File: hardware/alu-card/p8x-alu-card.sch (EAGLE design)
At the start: 32 parts, among them J1 DIN41612-96M, U1 A REG, U10 ALU HI, U11 CLA, U12 SH1 LO, U13 SH1 HI, U14 SH2 LO, U15 SH2 HI, U16 ALU OUT, U17 FLAGS, U18 Z DET, U19 74HCT08, U2 A OUT, U20 DOE DEC, U21 DLD DEC, U22 FLAG MUX, U23 FLAG OUT, U24 74HCT32, U25 74HCT00, U3 B REG, U4 B OUT, U5 T REG, U6 T OUT, U7 T2 REG, U8 T2 OUT, U9 ALU LO

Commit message: hw(rev B): ALU conventional-carry inverter; scope flag-reg redesign
Phase 2, step 4 (partial). The C flag is now conventional active-high:
the raw 74181 Cn+4 (active-low) is inverted by a spare U25 NAND gate
before the flag mux, matching the rev-B emulator/microcode.

The rest of the ALU rev-B work (LDZN independent Z/N latching, SETC/CLRC
forcing C, and the carry-coupled shifter) is one interlocking flag-
register redesign — it needs splitting C onto its own flip-flop and
source/clock muxes, ~6 chips that can only be pin-validated here, not
DRC'd. Scoped in detail in BACKLOG rather than bolted on unverified.
Functional behaviour is already proven in the emulator.

Co-Authored-By: Claude Opus 4.8 <noreply@anthropic.com>
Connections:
- new net CFLGI: U22.A1, U25.2Y
- net CFLG: now also U25.2A, U25.2B; no longer U22.A1
- net GND: no longer U25.2A, U25.2B
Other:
- note added: "P8X ALU CARD REV B-partial (carry conventional; flag-reg redesign pending - BACKLOG)"
- note removed: "P8X ALU CARD REV A (V FLAG UNIMPLEMENTED - SEE BACKLOG)"
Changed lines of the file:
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@@
 <part name="LED5" library="p8x" deviceset="LED" device="" value="LDF-YEL"/>
 </parts><sheets><sheet><plain>
-<text x="0" y="40" size="3.81" layer="97">P8X ALU CARD REV A (V FLAG UNIMPLEMENTED - SEE BACKLOG)</text>
+<text x="0" y="40" size="3.81" layer="97">P8X ALU CARD REV B-partial (carry conventional; flag-reg redesign pending - BACKLOG)</text>
 </plain><instances>
 <instance part="J1" gate="G$1" x="0" y="38.1"/>
@@
 <wire x1="259.38" y1="-251.46" x2="264.46" y2="-251.46" width="0.1524" layer="91"/>
 <label x="264.46" y="-250.95" size="1.778" layer="95"/></segment>
+<segment><pinref part="U25" gate="G$1" pin="2A"/>
+<wire x1="122.22" y1="-805.18" x2="117.14" y2="-805.18" width="0.1524" layer="91"/>
+<label x="117.14" y="-804.67" size="1.778" layer="95"/></segment>
+<segment><pinref part="U25" gate="G$1" pin="2B"/>
+<wire x1="122.22" y1="-807.72" x2="117.14" y2="-807.72" width="0.1524" layer="91"/>
+<label x="117.14" y="-807.21" size="1.778" layer="95"/></segment>
+</net>
+<net name="CFLGI" class="0">
+<segment><pinref part="U25" gate="G$1" pin="2Y"/>
+<wire x1="157.78" y1="-802.64" x2="162.86" y2="-802.64" width="0.1524" layer="91"/>
+<label x="162.86" y="-802.13" size="1.778" layer="95"/></segment>
 <segment><pinref part="U22" gate="G$1" pin="A1"/>
 <wire x1="223.82" y1="-662.94" x2="218.74" y2="-662.94" width="0.1524" layer="91"/>
@@
 <wire x1="427.02" y1="-678.18" x2="421.94" y2="-678.18" width="0.1524" layer="91"/>
 <label x="421.94" y="-677.67" size="1.778" layer="95"/></segment>
-<segment><pinref part="U25" gate="G$1" pin="2A"/>
-<wire x1="122.22" y1="-805.18" x2="117.14" y2="-805.18" width="0.1524" layer="91"/>
-<label x="117.14" y="-804.67" size="1.778" layer="95"/></segment>
-<segment><pinref part="U25" gate="G$1" pin="2B"/>
-<wire x1="122.22" y1="-807.72" x2="117.14" y2="-807.72" width="0.1524" layer="91"/>
-<label x="117.14" y="-807.21" size="1.778" layer="95"/></segment>
 <segment><pinref part="U25" gate="G$1" pin="4A"/>
 <wire x1="122.22" y1="-815.34" x2="117.14" y2="-815.34" width="0.1524" layer="91"/>

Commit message: hw(rev B): ALU flag-register redesign — completes Phase 2
Splits the flag register so the rev-B controls work in hardware:
- C flag on its own 7474 (U26), clocked CLK&LDF; SETC/CLRC drive its
  async preset/clear (via U25 NAND inverters + U31 AND with -RES).
- C source mux (U28/U29 74157): shifted-out bit (F7 if SH0, F0 if SH1)
  when shifting, else the inverted Cn+4 (conventional carry).
- shifter shift-in mux (U30 74157): current C when SHCIN else CIN.
- Z/N/V kept in U17 (74175), clocked CLK&(LDF|LDZN); on LDZN their source
  mux U22 selects a 74260 bus zero-detect (U27) and D7 instead of the ALU
  result, so loads set Z/N without disturbing C/V. The unused flag-restore
  (DLD=5) mux was repurposed for this.
ALU card retitled REV B; LDZN/SHCIN/SETC/CLRC added to its bus set.
Validates clean (pin/pad); behaviour proven in the emulator. BACKLOG
marks Phase 2 done; full Eagle DRC stays on VERIFY.

Co-Authored-By: Claude Opus 4.8 <noreply@anthropic.com>
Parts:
- added U26: C FLAG FF, p8x:7474
- added U27: BUS Z-DET, p8x:74260
- added U28: SHIFT-OUT MUX, p8x:74157
- added U29: C-SRC MUX, p8x:74157
- added U30: SHIN MUX, p8x:74157
- added U31: 74HCT08 CLK/FORCE, p8x:GATES14
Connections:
- net FM0 renamed ZSRC
- net FM1 renamed NSRC
- removed net -FREST: U21.Y5, U25.1A, U25.1B
- removed net CLKF: U17.CLK, U19.2Y
- removed net FEN: U19.2B, U24.1Y
- removed net FM2: U17.D3, U22.Y3
- removed net FM3: U17.D4, U22.Y4
- removed net FRESP: U22.S, U24.1B, U25.1Y
- new net -CCLR: U26.!1CLR, U31.3Y
- new net -CLRCb: U25.4Y, U31.3B
- new net -SETCb: U25.1Y, U26.!1PRE
- new net CLKFC: U26.1CLK, U31.1Y
- new net CLKFZN: U17.CLK, U31.2Y
- new net CLRC: J1.B27, U25.4A, U25.4B
- new net FENZN: U24.1Y, U31.2A
- new net LDZN: J1.C28, U22.S, U24.1B
- new net NC: U26.1D, U29.Y1
- new net SETC: J1.C30, U25.1A, U25.1B
- new net SHANY: U24.2Y, U29.S
- new net SHCIN: J1.C29, U30.S
- new net SHIN: U12.B1, U15.B4, U30.Y1
- new net SHOUT: U28.Y1, U29.B1
- new net ZBH: U19.2B, U27.Y2
- new net ZBL: U19.2A, U27.Y1
- new net ZBUS: U19.2Y, U22.B1
- net -RES: now also U31.3A
- net CFLGI: now also U29.A1; no longer U22.A1
- net CIN: now also U30.A1; no longer U12.B1, U15.B4
- net CLK: now also U31.1A, U31.2B; no longer U19.2A
- net D0: now also U27.A1; no longer U22.B1
- net D1: now also U27.B1; no longer U22.B2
- net D2: now also U27.C1; no longer U22.B3
- net D3: now also U27.D1; no longer U22.B4
- net D4: now also U27.E1
- net D5: now also U27.A2
- net D6: now also U27.B2
- net D7: now also U22.B2, U27.C2
- net F0: now also U28.A1
- net F7: now also U28.B1
- net FQC: now also U26.1Q, U30.B1; no longer U17.Q1
- net FQN: now also U17.Q2; no longer U17.Q3
- net FQV: now also U17.Q3; no longer U17.Q4
- net FQZ: now also U17.Q1; no longer U17.Q2
- net GND: now also U17.D3, U26.2CLK, U26.2D, U27.D2, U27.E2, U28.!G, U29.!G, U30.!G, U31.4A, U31.4B; no longer U22.A4, U24.2A, U24.2B, U25.4A, U25.4B
- net LDF: now also U31.1B
- net R7: now also U22.A2; no longer U22.A3
- net SH0: now also U24.2A, U28.S
- net SH1: now also U24.2B
- net VCC: now also U26.!2CLR, U26.!2PRE
- net ZFLG: now also U22.A1; no longer U22.A2
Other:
- note added: "P8X ALU CARD REV B (conventional carry, LDZN, SETC/CLRC, carry-coupled shifter)"
- note removed: "P8X ALU CARD REV B-partial (carry conventional; flag-reg redesign pending - BACKLOG)"
- moved on the sheet: LED3, LED4, LED5, R4, R5, RP1

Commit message: hw: per-IC 100nF decoupling caps on every card
card standards sec.5 requires a decoupling cap per IC; only the backplane had
them. gen_eagle's card() now generates one 100nF cap (CDn, C_DISC footprint)
per IC on the five plug-in cards, placed next to its IC and wired VCC<->GND;
the memory card's separate build does the same for U1-U9.

Caps added: control 18, regbank 44, alu 31, io 15, cf 8, memory 9. All 7
boards regenerate with 0 validation errors; card schematic PDFs refreshed.
Placement is approximate (caps sit just below each IC) pending Fusion routing.

Clears a pre-fab blocker from the backlog.

Co-Authored-By: Claude Opus 4.8 <noreply@anthropic.com>
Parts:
- added CD1, CD10, CD11, CD12, CD13, CD14, CD15, CD16, CD17, CD18, CD19, CD2, CD20, CD21, CD22, CD23, CD24, CD25, CD26, CD27, CD28, CD29, CD3, CD30, CD31, CD4, CD5, CD6, CD7, CD8, CD9: 100N, p8x:CAP
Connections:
- net GND: now also CD1.2, CD10.2, CD11.2, CD12.2, CD13.2, CD14.2, CD15.2, CD16.2, CD17.2, CD18.2, CD19.2, CD2.2, CD20.2, CD21.2, CD22.2, CD23.2, CD24.2, CD25.2, CD26.2, CD27.2, CD28.2, CD29.2, CD3.2, CD30.2, CD31.2, CD4.2, CD5.2, CD6.2, CD7.2, CD8.2, CD9.2
- net VCC: now also CD1.1, CD10.1, CD11.1, CD12.1, CD13.1, CD14.1, CD15.1, CD16.1, CD17.1, CD18.1, CD19.1, CD2.1, CD20.1, CD21.1, CD22.1, CD23.1, CD24.1, CD25.1, CD26.1, CD27.1, CD28.1, CD29.1, CD3.1, CD30.1, CD31.1, CD4.1, CD5.1, CD6.1, CD7.1, CD8.1, CD9.1

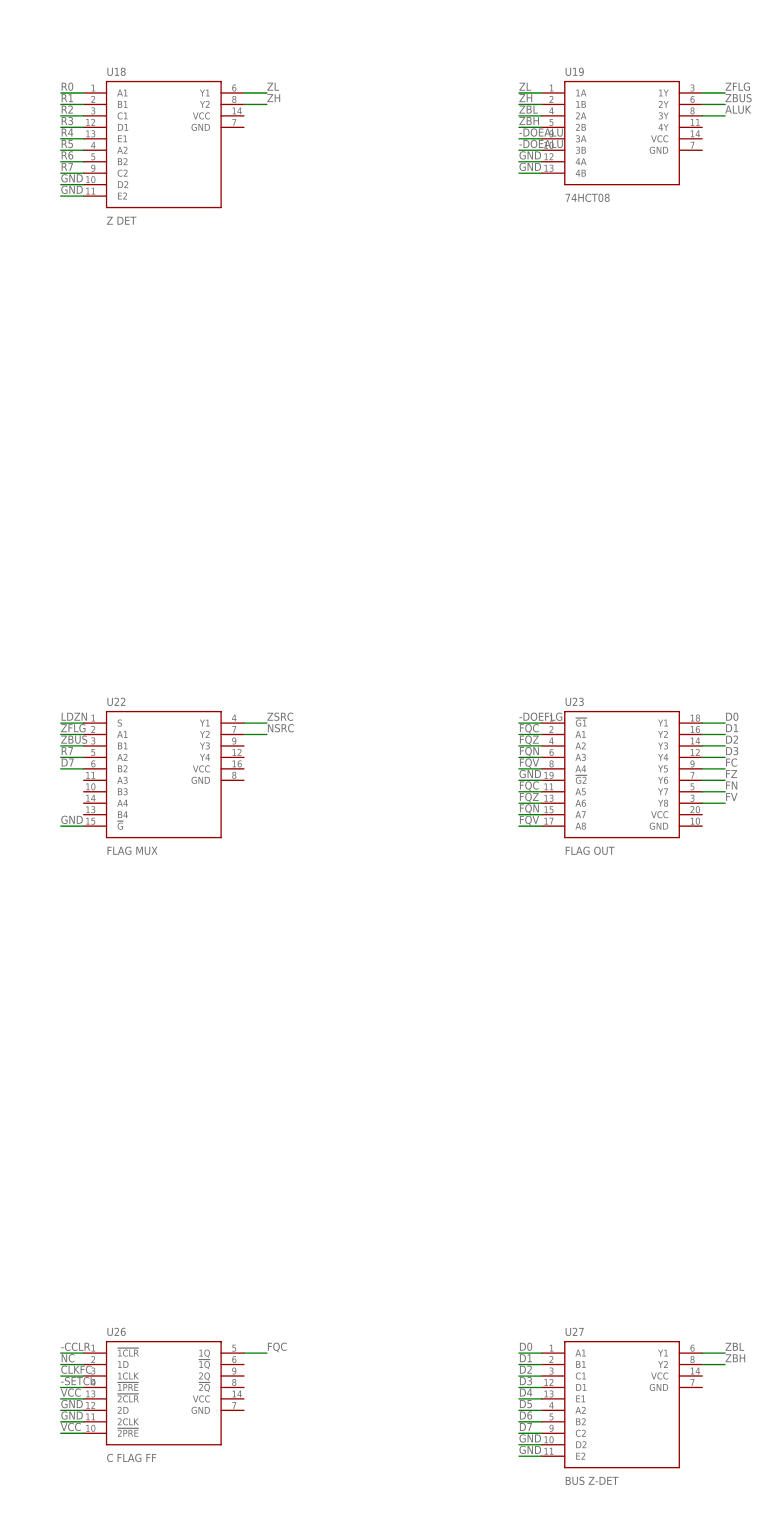
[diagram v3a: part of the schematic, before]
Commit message: hw: fix 74260 pinout (ALU zero-detect); datasheet pinout audit
Audited all ~25 device pin maps in gen_eagle's library against standard
datasheet pinouts. Found one real error: 74260 (dual 5-input NOR, used as the
ALU bus zero-detect U27) had a scrambled pin map — gate-1 C1 on pin 3 (should
be 11) and the Y1/Y2 outputs swapped (6<->8). Corrected to the datasheet
(1=1A 2=1B 3=2A 4=2B 5=2C 6=2Y 7=GND 8=1Y 9=2D 10=2E 11=1C 12=1D 13=1E 14=VCC);
netlist uses logical pin names so it's unchanged, and the zero-detect now wires
to the right pins. All other devices matched. Boards + PDFs regenerated, 0
validation errors.

Left a VERIFY note to confirm against physical datasheets before fab.

Co-Authored-By: Claude Opus 4.8 <noreply@anthropic.com>
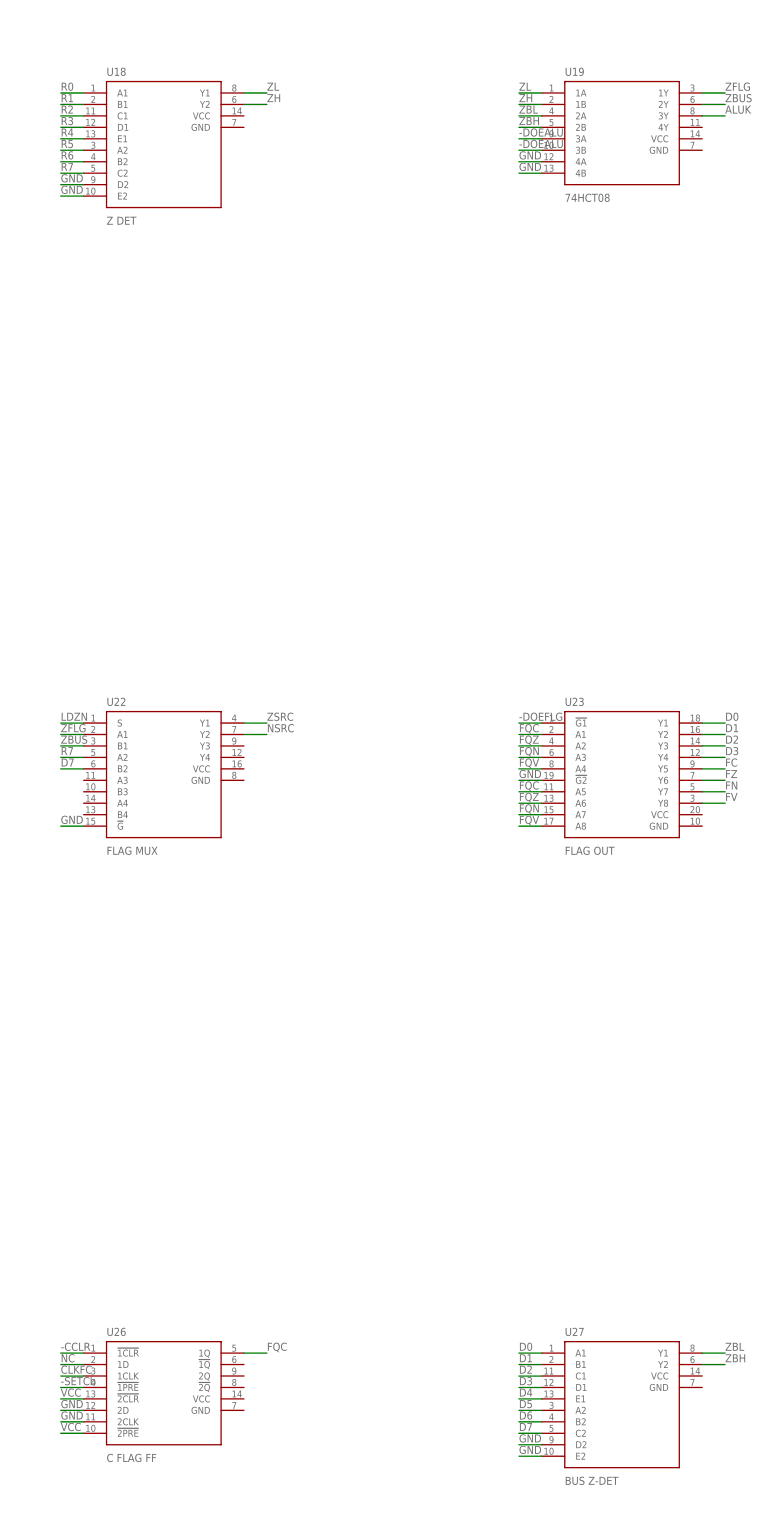
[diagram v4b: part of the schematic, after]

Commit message: feat: 2nd ALU-input mux (rev C) — B-side operand can select T
Add a 2:1 mux on the ALU B-operand path so the second ALU operand can be
the T register instead of B, controlled by a new microcode-word bit.

- microcode (genucode.py): BSEL = word bit 31 (was the lone spare); new
  opcodes ADDT/SUBT/ANDT/ORT/XORT/CMPT (0x80-0x85) run the ALU with T as
  the B operand (B preserved); LDT #imm / LDT a (0x86/0x87) expose T, which
  was microcode-scratch-only and had no programmer-visible load.
- emulator (p8xemu.c): decode bit 31; ALU B operand = bsel ? T : B.
- hardware (gen_eagle.py): ALU card U32/U33 (74157 x2) mux BQ vs TQ -> 74181 B;
  BSEL latched in control-card pipe U17.Q8, carried on backplane B28 (was
  SPARE9). All 7 boards regenerate with 0 validation errors.
- bus map kept consistent across both generators (gen_eagle.py, gen_bus_pdf.py),
  the backplane render, and the hardware docs (bus-definition is authoritative).
- tests: new ISA coverage for the T-operand ops (sentinel wrong-operand bait);
  all 6 suites pass.
- docs: programmer's guide regenerated; BACKLOG updated (mux -> DONE; added a
  post-bringup idea to optimize monitor/OS/BASIC hot paths with the T ops).

Backward-compatible: no existing opcode changed; BSEL defaults 0 (= B register),
so existing monitor/OS/BASIC binaries are byte-identical.

Co-Authored-By: Claude Opus 4.8 <noreply@anthropic.com>
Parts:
- added CD32, CD33: 100N, p8x:CAP
- added U32: B-MUX LO, p8x:74157
- added U33: B-MUX HI, p8x:74157
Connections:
- new net BMX0: U32.Y1, U9.B0
- new net BMX1: U32.Y2, U9.B1
- new net BMX2: U32.Y3, U9.B2
- new net BMX3: U32.Y4, U9.B3
- new net BMX4: U10.B0, U33.Y1
- new net BMX5: U10.B1, U33.Y2
- new net BMX6: U10.B2, U33.Y3
- new net BMX7: U10.B3, U33.Y4
- new net BSEL: J1.B28, U32.S, U33.S
- net BQ0: now also U32.A1; no longer U9.B0
- net BQ1: now also U32.A2; no longer U9.B1
- net BQ2: now also U32.A3; no longer U9.B2
- net BQ3: now also U32.A4; no longer U9.B3
- net BQ4: now also U33.A1; no longer U10.B0
- net BQ5: now also U33.A2; no longer U10.B1
- net BQ6: now also U33.A3; no longer U10.B2
- net BQ7: now also U33.A4; no longer U10.B3
- net GND: now also CD32.2, CD33.2, U32.!G, U33.!G
- net TQ0: now also U32.B1
- net TQ1: now also U32.B2
- net TQ2: now also U32.B3
- net TQ3: now also U32.B4
- net TQ4: now also U33.B1
- net TQ5: now also U33.B2
- net TQ6: now also U33.B3
- net TQ7: now also U33.B4
- net VCC: now also CD32.1, CD33.1
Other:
- moved on the sheet: CD1, CD10, CD11, CD12, CD13, CD14, CD15, CD16, CD17, CD18, CD19, CD2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

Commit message: feat: V flag + signed comparison branches (rev C)
Implement signed overflow (V) and signed-compare branches end to end, so the
machine can do signed ordering (C alone only gives unsigned).

Hardware (the old "one 7486 from carry-in vs carry-out of bit 7" plan was not
feasible: a 74181 4-bit group doesn't expose carry-into-bit-7). Sign-bit method:
  V = (A7 ^ F7) & (A7 ^ B7 ^ ~ALUS2)
  (B7 = muxed B operand, F7 = raw ALU result sign; isADD = ~S2). Ungated by M,
  so V is valid after ADD/SUB/CMP.
- ALU card: U34 (74HCT86) + U35 (74HCT08) derive V into the flag register
  (was tied low). FV already bused, no bus change.
- control card: U19 (74HCT86) -> N^V on cond-mux D6; spare U6 OR gate ->
  (N^V)|Z on D7 (both were grounded). FCOND 6/7 select them.

Microcode: BLT/BGE/BLE/BGT (0x44-0x47), FC LT=6 (N^V), LE=7 ((N^V)|Z).
Emulator: computes V by the identical Boolean; cond cases 6/7 added.
Tests: ISA coverage for sign-boundary cases unsigned C gets wrong (e.g. -128<1).
Docs: programmer's guide + BACKLOG (V flag VERIFY -> DONE).

All 7 boards regenerate with 0 validation errors; all 6 test suites pass.

Co-Authored-By: Claude Opus 4.8 <noreply@anthropic.com>
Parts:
- added CD34, CD35: 100N, p8x:CAP
- added U34: 74HCT86 V-XOR, p8x:GATES14
- added U35: 74HCT08 V-AND, p8x:GATES14
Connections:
- new net NS2: U34.3Y, U34.4B
- new net VSRC: U17.D3, U35.1Y
- new net VX1: U34.1Y, U35.1A
- new net VX2: U34.2Y, U34.4A
- new net VX4: U34.4Y, U35.1B
- net ALUS2: now also U34.3A
- net AQ7: now also U34.1A, U34.2A
- net BMX7: now also U34.2B
- net F7: now also U34.1B
- net GND: now also CD34.2, CD35.2, U35.2A, U35.2B, U35.3A, U35.3B, U35.4A, U35.4B; no longer U17.D3
- net VCC: now also CD34.1, CD35.1, U34.3B
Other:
- moved on the sheet: CD1, CD10, CD11, CD12, CD13, CD14, CD15, CD16, CD17, CD18, CD19, CD2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

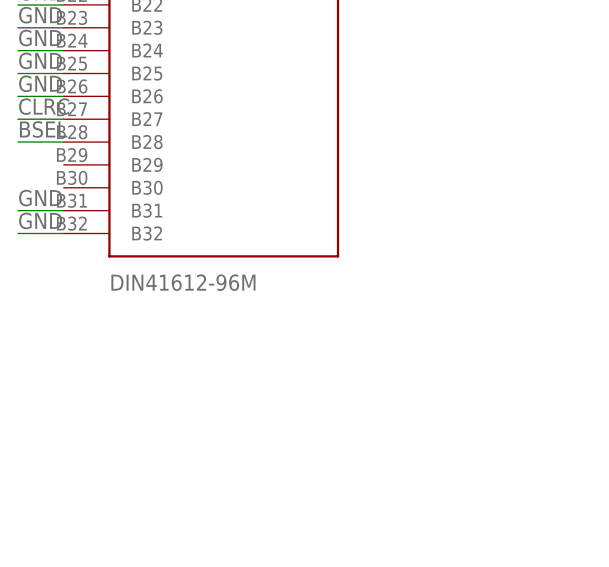
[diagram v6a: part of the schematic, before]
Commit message: fix(bom): card DIN connectors were undercounted (1 -> 6); label them FABC96R
Two fixes:
- card() built CARDS[name] from `allp`, which omitted J1 — so the 5 plug-in
  cards' DIN41612 edge connectors never reached the BOM (it showed qty 1, only
  the memory card's J1). Include J1 in allp (the schematic renderer already
  filters J1 by name, so rendering is unchanged). BOM now correctly shows 6 card
  connectors + 10 backplane receptacles.
- Card edge connector is FABC96R (user-specified): set the value label on every
  card J1 and name it in the BOM; backplane receptacles noted as the mating part.

Regenerated all boards + PDFs + BOM; all 6 test suites pass.

Co-Authored-By: Claude Opus 4.8 <noreply@anthropic.com>
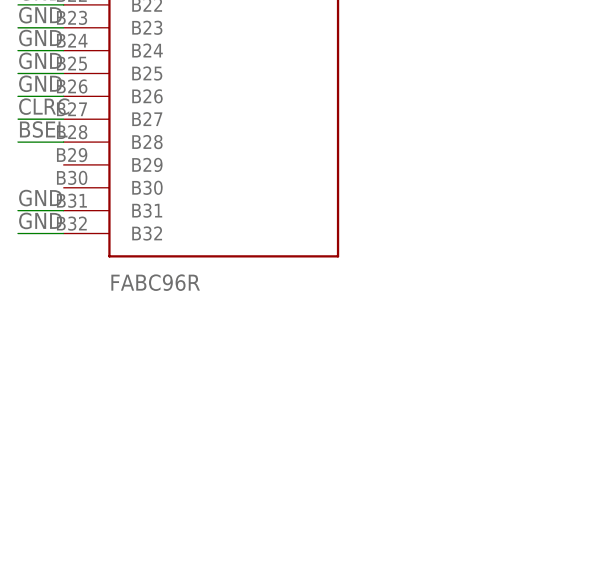
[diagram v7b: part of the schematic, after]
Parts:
- J1: value DIN41612-96M -> FABC96R
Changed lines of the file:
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@@
 <classes><class number="0" name="default" width="0" drill="0"/></classes>
 <parts>
-<part name="J1" library="p8x" deviceset="DIN96" device="" value="DIN41612-96M"/>
+<part name="J1" library="p8x" deviceset="DIN96" device="" value="FABC96R"/>
 <part name="U1" library="p8x" deviceset="74377V2" device="" value="A REG"/>
 <part name="U2" library="p8x" deviceset="74244" device="" value="A OUT"/>

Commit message: fix(hardware): connect IC power pins on the card()-built boards
Schematic-review fix. card() wired the edge-connector and decoupling-cap pins to
VCC/GND but never added each IC's own VCC/GND supply pin, so on control, regbank,
ALU, I/O, and CF the chips' power pads were not members of the power pours and
would not have been powered. (The hand-built memory card already did this; the
backplane has no ICs. validate() couldn't catch it — it checks pin-name legality,
not connectivity.)

- card(): append (ref,"VCC")/(ref,"GND") for every IC, skipping any pin already
  wired by hand (idempotent — avoids duplicate pinrefs, e.g. ALU U16 GND)
- regenerated all 7 boards (.sch/.brd), 0 validation errors
- board-level audit: every IC on every card now has both VCC and GND on the
  power signals
- BACKLOG: moved the critical item to DONE; theory docs' power-pin callouts
  updated to "fixed"

Co-Authored-By: Claude Opus 4.8 <noreply@anthropic.com>
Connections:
- net GND: now also U1.GND, U10.GND, U11.GND, U12.GND, U13.GND, U14.GND, U15.GND, U16.GND, U17.GND, U18.GND, U19.GND, U2.GND, U20.GND, U21.GND, U22.GND, U23.GND, U24.GND, U25.GND, U26.GND, U27.GND, U28.GND, U29.GND, U3.GND, U30.GND, U31.GND, U32.GND, U33.GND, U34.GND, U35.GND, U4.GND, U5.GND, U6.GND, U7.GND, U8.GND, U9.GND
- net VCC: now also U1.VCC, U10.VCC, U11.VCC, U12.VCC, U13.VCC, U14.VCC, U15.VCC, U16.VCC, U17.VCC, U18.VCC, U19.VCC, U2.VCC, U20.VCC, U21.VCC, U22.VCC, U23.VCC, U24.VCC, U25.VCC, U26.VCC, U27.VCC, U28.VCC, U29.VCC, U3.VCC, U30.VCC, U31.VCC, U32.VCC, U33.VCC, U34.VCC, U35.VCC, U4.VCC, U5.VCC, U6.VCC, U7.VCC, U8.VCC, U9.VCC
